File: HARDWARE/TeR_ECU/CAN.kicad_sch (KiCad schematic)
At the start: 7 parts, among them U1 SN65HVD230

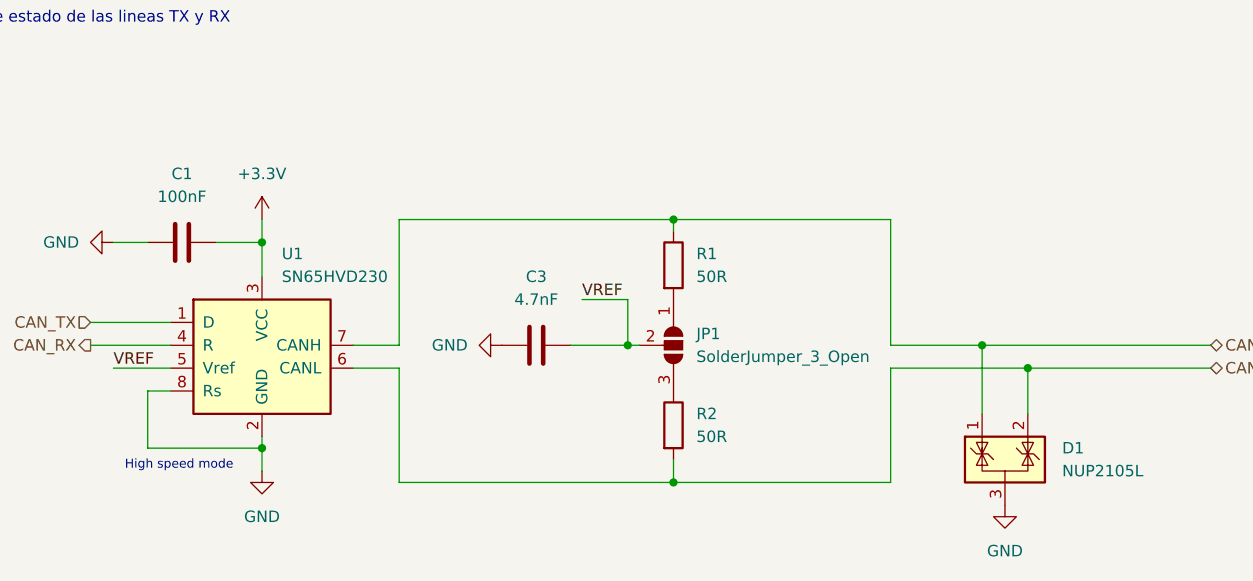
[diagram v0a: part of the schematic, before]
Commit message: Rethought layout and footprints and fixed fuse normative problem
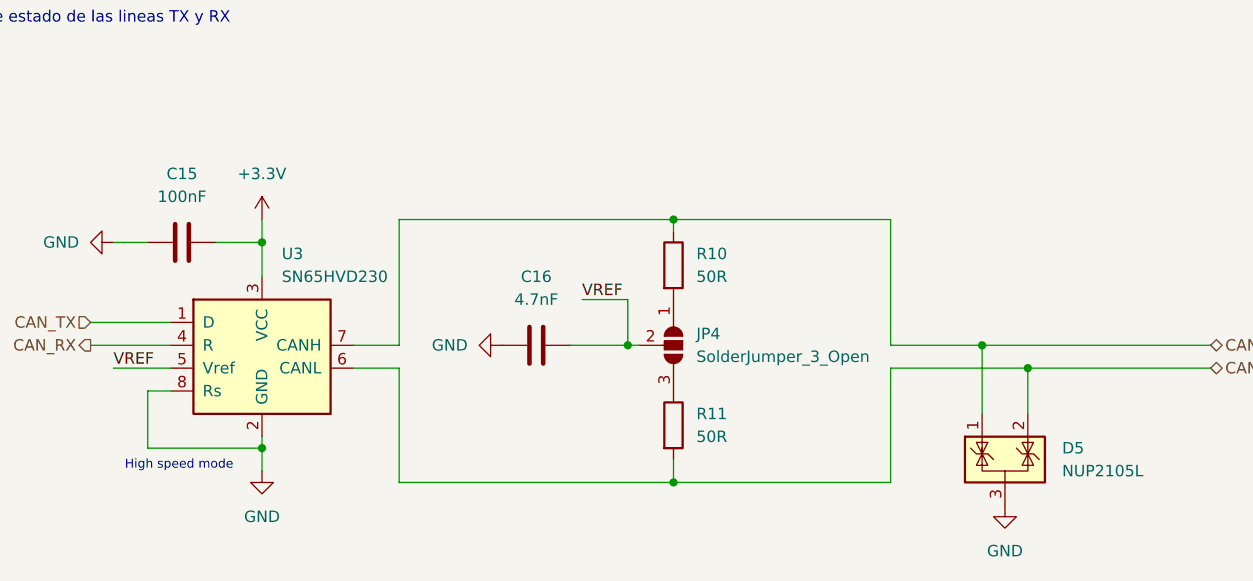
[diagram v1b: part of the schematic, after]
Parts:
- renumbered C1 to C15, C3 to C16, D1 to D5, JP1 to JP4, R1 to R10, R2 to R11, U1 to U3
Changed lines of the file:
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@@
   (symbol (lib_id "power:GND") (at 77.47 73.66 270) (unit 1)
     (in_bom yes) (on_board yes) (dnp no) (fields_autoplaced)
-    (property "Reference" "#PWR03" (at 71.12 73.66 0)
+    (property "Reference" "#PWR031" (at 71.12 73.66 0)
       (effects (font (size 1.27 1.27)) hide)
     )
@@
       (project "TeR_ECU"
         (path "/84413845-c4f3-4743-bcd2-a67649c90902/277954e6-e504-4754-bfff-78bccbfcfb29"
-          (reference "#PWR03") (unit 1)
-        )
-        (path "/84413845-c4f3-4743-bcd2-a67649c90902/5e77d980-0e17-4264-b0d2-78c6bd2786ec"
-          (reference "#PWR05") (unit 1)
+          (reference "#PWR031") (unit 1)
+        )
+        (path "/84413845-c4f3-4743-bcd2-a67649c90902/5e77d980-0e17-4264-b0d2-78c6bd2786ec"
+          (reference "#PWR024") (unit 1)
         )
       )
@@
   (symbol (lib_id "Device:R") (at 139.7 76.2 0) (unit 1)
     (in_bom yes) (on_board yes) (dnp no) (fields_autoplaced)
-    (property "Reference" "R1" (at 142.24 74.93 0)
+    (property "Reference" "R10" (at 142.24 74.93 0)
       (effects (font (size 1.27 1.27)) (justify left))
     )
@@
       (project "TeR_ECU"
         (path "/84413845-c4f3-4743-bcd2-a67649c90902/277954e6-e504-4754-bfff-78bccbfcfb29"
-          (reference "R1") (unit 1)
-        )
-        (path "/84413845-c4f3-4743-bcd2-a67649c90902/5e77d980-0e17-4264-b0d2-78c6bd2786ec"
-          (reference "R3") (unit 1)
+          (reference "R10") (unit 1)
+        )
+        (path "/84413845-c4f3-4743-bcd2-a67649c90902/5e77d980-0e17-4264-b0d2-78c6bd2786ec"
+          (reference "R8") (unit 1)
         )
       )
@@
   (symbol (lib_id "power:GND") (at 120.65 85.09 270) (unit 1)
     (in_bom yes) (on_board yes) (dnp no) (fields_autoplaced)
-    (property "Reference" "#PWR09" (at 114.3 85.09 0)
+    (property "Reference" "#PWR032" (at 114.3 85.09 0)
       (effects (font (size 1.27 1.27)) hide)
     )
@@
       (project "TeR_ECU"
         (path "/84413845-c4f3-4743-bcd2-a67649c90902/277954e6-e504-4754-bfff-78bccbfcfb29"
-          (reference "#PWR09") (unit 1)
-        )
-        (path "/84413845-c4f3-4743-bcd2-a67649c90902/5e77d980-0e17-4264-b0d2-78c6bd2786ec"
-          (reference "#PWR08") (unit 1)
+          (reference "#PWR032") (unit 1)
+        )
+        (path "/84413845-c4f3-4743-bcd2-a67649c90902/5e77d980-0e17-4264-b0d2-78c6bd2786ec"
+          (reference "#PWR025") (unit 1)
         )
       )
@@
   (symbol (lib_id "Device:R") (at 139.7 93.98 0) (unit 1)
     (in_bom yes) (on_board yes) (dnp no) (fields_autoplaced)
-    (property "Reference" "R2" (at 142.24 92.71 0)
+    (property "Reference" "R11" (at 142.24 92.71 0)
       (effects (font (size 1.27 1.27)) (justify left))
     )
@@
       (project "TeR_ECU"
         (path "/84413845-c4f3-4743-bcd2-a67649c90902/277954e6-e504-4754-bfff-78bccbfcfb29"
-          (reference "R2") (unit 1)
-        )
-        (path "/84413845-c4f3-4743-bcd2-a67649c90902/5e77d980-0e17-4264-b0d2-78c6bd2786ec"
-          (reference "R4") (unit 1)
+          (reference "R11") (unit 1)
+        )
+        (path "/84413845-c4f3-4743-bcd2-a67649c90902/5e77d980-0e17-4264-b0d2-78c6bd2786ec"
+          (reference "R9") (unit 1)
         )
       )
@@
   (symbol (lib_id "power:+3.3V") (at 93.98 71.12 0) (unit 1)
     (in_bom yes) (on_board yes) (dnp no) (fields_autoplaced)
-    (property "Reference" "#PWR02" (at 93.98 74.93 0)
+    (property "Reference" "#PWR030" (at 93.98 74.93 0)
       (effects (font (size 1.27 1.27)) hide)
     )
@@
       (project "TeR_ECU"
         (path "/84413845-c4f3-4743-bcd2-a67649c90902/277954e6-e504-4754-bfff-78bccbfcfb29"
-          (reference "#PWR02") (unit 1)
-        )
-        (path "/84413845-c4f3-4743-bcd2-a67649c90902/5e77d980-0e17-4264-b0d2-78c6bd2786ec"
-          (reference "#PWR06") (unit 1)
+          (reference "#PWR030") (unit 1)
+        )
+        (path "/84413845-c4f3-4743-bcd2-a67649c90902/5e77d980-0e17-4264-b0d2-78c6bd2786ec"
+          (reference "#PWR023") (unit 1)
         )
       )
@@
   (symbol (lib_id "Device:C") (at 124.46 85.09 270) (unit 1)
     (in_bom yes) (on_board yes) (dnp no) (fields_autoplaced)
-    (property "Reference" "C3" (at 124.46 77.47 90)
+    (property "Reference" "C16" (at 124.46 77.47 90)
       (effects (font (size 1.27 1.27)))
     )
@@
       (project "TeR_ECU"
         (path "/84413845-c4f3-4743-bcd2-a67649c90902/277954e6-e504-4754-bfff-78bccbfcfb29"
-          (reference "C3") (unit 1)
-        )
-        (path "/84413845-c4f3-4743-bcd2-a67649c90902/5e77d980-0e17-4264-b0d2-78c6bd2786ec"
-          (reference "C4") (unit 1)
+          (reference "C16") (unit 1)
+        )
+        (path "/84413845-c4f3-4743-bcd2-a67649c90902/5e77d980-0e17-4264-b0d2-78c6bd2786ec"
+          (reference "C14") (unit 1)
         )
       )
@@
   (symbol (lib_id "power:GND") (at 176.53 102.87 0) (unit 1)
     (in_bom yes) (on_board yes) (dnp no) (fields_autoplaced)
-    (property "Reference" "#PWR04" (at 176.53 109.22 0)
+    (property "Reference" "#PWR034" (at 176.53 109.22 0)
       (effects (font (size 1.27 1.27)) hide)
     )
@@
       (project "TeR_ECU"
         (path "/84413845-c4f3-4743-bcd2-a67649c90902/277954e6-e504-4754-bfff-78bccbfcfb29"
-          (reference "#PWR04") (unit 1)
-        )
-        (path "/84413845-c4f3-4743-bcd2-a67649c90902/5e77d980-0e17-4264-b0d2-78c6bd2786ec"
-          (reference "#PWR010") (unit 1)
+          (reference "#PWR034") (unit 1)
+        )
+        (path "/84413845-c4f3-4743-bcd2-a67649c90902/5e77d980-0e17-4264-b0d2-78c6bd2786ec"
+          (reference "#PWR027") (unit 1)
         )
       )
@@
   (symbol (lib_id "Device:C") (at 85.09 73.66 90) (unit 1)
     (in_bom yes) (on_board yes) (dnp no) (fields_autoplaced)
-    (property "Reference" "C1" (at 85.09 66.04 90)
+    (property "Reference" "C15" (at 85.09 66.04 90)
       (effects (font (size 1.27 1.27)))
     )
@@
       (project "TeR_ECU"
         (path "/84413845-c4f3-4743-bcd2-a67649c90902/277954e6-e504-4754-bfff-78bccbfcfb29"
-          (reference "C1") (unit 1)
-        )
-        (path "/84413845-c4f3-4743-bcd2-a67649c90902/5e77d980-0e17-4264-b0d2-78c6bd2786ec"
-          (reference "C2") (unit 1)
+          (reference "C15") (unit 1)
+        )
+        (path "/84413845-c4f3-4743-bcd2-a67649c90902/5e77d980-0e17-4264-b0d2-78c6bd2786ec"
+          (reference "C13") (unit 1)
         )
       )
@@
   (symbol (lib_id "power:GND") (at 93.98 99.06 0) (unit 1)
     (in_bom yes) (on_board yes) (dnp no) (fields_autoplaced)
-    (property "Reference" "#PWR01" (at 93.98 105.41 0)
+    (property "Reference" "#PWR033" (at 93.98 105.41 0)
       (effects (font (size 1.27 1.27)) hide)
     )
@@
       (project "TeR_ECU"
         (path "/84413845-c4f3-4743-bcd2-a67649c90902/277954e6-e504-4754-bfff-78bccbfcfb29"
-          (reference "#PWR01") (unit 1)
-        )
-        (path "/84413845-c4f3-4743-bcd2-a67649c90902/5e77d980-0e17-4264-b0d2-78c6bd2786ec"
-          (reference "#PWR07") (unit 1)
+          (reference "#PWR033") (unit 1)
+        )
+        (path "/84413845-c4f3-4743-bcd2-a67649c90902/5e77d980-0e17-4264-b0d2-78c6bd2786ec"
+          (reference "#PWR026") (unit 1)
         )
       )
@@
   (symbol (lib_id "Interface_CAN_LIN:SN65HVD230") (at 93.98 85.09 0) (unit 1)
     (in_bom yes) (on_board yes) (dnp no) (fields_autoplaced)
-    (property "Reference" "U1" (at 96.1741 74.93 0)
+    (property "Reference" "U3" (at 96.1741 74.93 0)
       (effects (font (size 1.27 1.27)) (justify left))
     )
@@
       (project "TeR_ECU"
         (path "/84413845-c4f3-4743-bcd2-a67649c90902/277954e6-e504-4754-bfff-78bccbfcfb29"
-          (reference "U1") (unit 1)
+          (reference "U3") (unit 1)
         )
         (path "/84413845-c4f3-4743-bcd2-a67649c90902/5e77d980-0e17-4264-b0d2-78c6bd2786ec"
@@
   (symbol (lib_id "Power_Protection:NUP2105L") (at 176.53 97.79 0) (unit 1)
     (in_bom yes) (on_board yes) (dnp no) (fields_autoplaced)
-    (property "Reference" "D1" (at 182.88 96.52 0)
+    (property "Reference" "D5" (at 182.88 96.52 0)
       (effects (font (size 1.27 1.27)) (justify left))
     )
@@
       (project "TeR_ECU"
         (path "/84413845-c4f3-4743-bcd2-a67649c90902/277954e6-e504-4754-bfff-78bccbfcfb29"
-          (reference "D1") (unit 1)
-        )
-        (path "/84413845-c4f3-4743-bcd2-a67649c90902/5e77d980-0e17-4264-b0d2-78c6bd2786ec"
-          (reference "D2") (unit 1)
+          (reference "D5") (unit 1)
+        )
+        (path "/84413845-c4f3-4743-bcd2-a67649c90902/5e77d980-0e17-4264-b0d2-78c6bd2786ec"
+          (reference "D4") (unit 1)
         )
       )
@@
   (symbol (lib_id "Jumper:SolderJumper_3_Open") (at 139.7 85.09 270) (unit 1)
     (in_bom yes) (on_board yes) (dnp no) (fields_autoplaced)
-    (property "Reference" "JP1" (at 142.24 83.82 90)
+    (property "Reference" "JP4" (at 142.24 83.82 90)
       (effects (font (size 1.27 1.27)) (justify left))
     )
@@
       (project "TeR_ECU"
         (path "/84413845-c4f3-4743-bcd2-a67649c90902/277954e6-e504-4754-bfff-78bccbfcfb29"
-          (reference "JP1") (unit 1)
-        )
-        (path "/84413845-c4f3-4743-bcd2-a67649c90902/5e77d980-0e17-4264-b0d2-78c6bd2786ec"
-          (reference "JP2") (unit 1)
-        )
-      )
+          (reference "JP4") (unit 1)
+        )
+        (path "/84413845-c4f3-4743-bcd2-a67649c90902/5e77d980-0e17-4264-b0d2-78c6bd2786ec"
+          (reference "JP3") (unit 1)
+        )
+      )

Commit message: Kept improving schmatic for V2
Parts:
- removed D5: NUP2105L, Package_TO_SOT_SMD:SOT-23, symbol Power_Protection:NUP2105L
- removed JP4: SolderJumper_3_Open, Jumper:SolderJumper-3_P1.3mm_Open_Pad1.0x1.5mm, symbol Jumper:SolderJumper_3_Open
- removed R11: 50R, Resistor_SMD:R_0805_2012Metric, symbol Device:R
- added D2: NUP2105L, Package_TO_SOT_SMD:SOT-23, symbol Power_Protection:NUP2105L
- added FL2: ACT45B-510-2P-TL003, ACT45B-510-2P-TL003:FIL_ACT45B-510-2P-TL003, symbol CAN_CMF:ACT45B-510-2P-TL003
- added JP2: SolderJumper_3_Open, Jumper:SolderJumper-3_P1.3mm_Open_Pad1.0x1.5mm, symbol Jumper:SolderJumper_3_Open
- added R9: 50R, Resistor_SMD:R_0805_2012Metric, symbol Device:R
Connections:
- net CAN+: now also FL2.2, R9.1; no longer R10.1, U3.7 (CANH)
- net CAN-: now also R10.2, FL2.1; no longer U3.6 (CANL)
- net GND: now also D2.3 (A)
- net VREF: now also JP2.2 (C)
- new net: JP2.1 (A), R9.2
- new net: JP2.3 (B), R10.1
- new net: D2.1 (K), FL2.4, U3.6 (CANL)
- new net: D2.2 (K), FL2.3, U3.7 (CANH)
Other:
- note added: "Isolated Can Bus transceiver"
- note removed: "Valorar leds de estado de las lineas TX y RX"

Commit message: Quick changes
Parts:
- added C24, C25: 100p, symbol Device:C
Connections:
- net CAN+: now also C25.1
- net CAN-: now also C24.1
- net GND: now also C24.2, C25.2

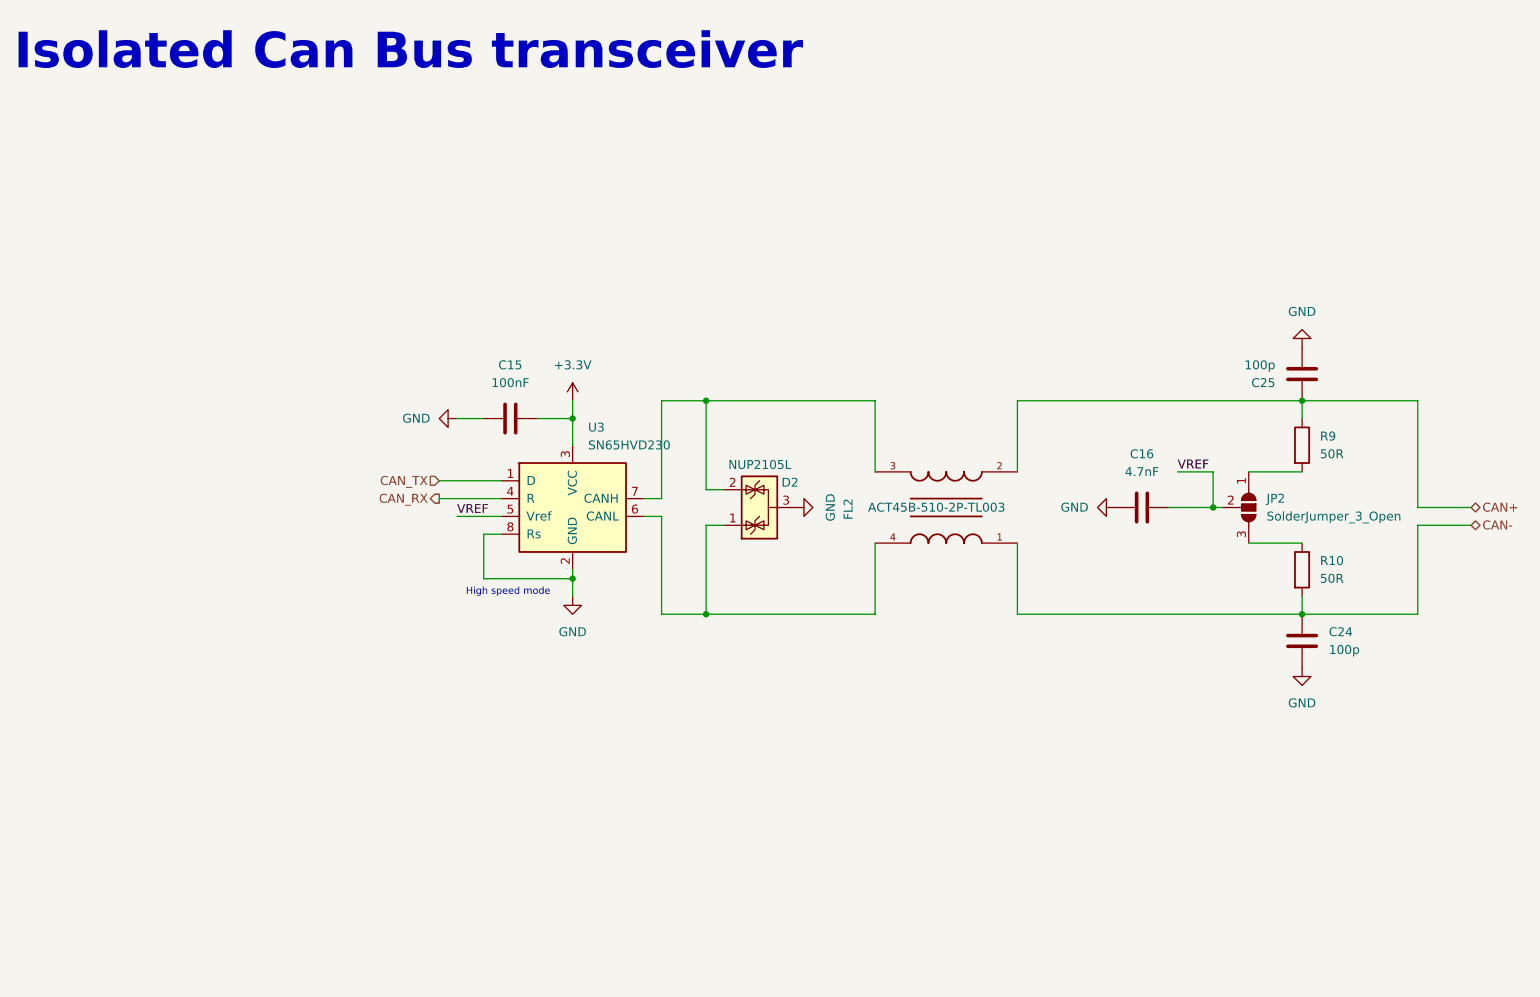
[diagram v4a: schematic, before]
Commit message: Advanced design and added IMU/GPS moduleç
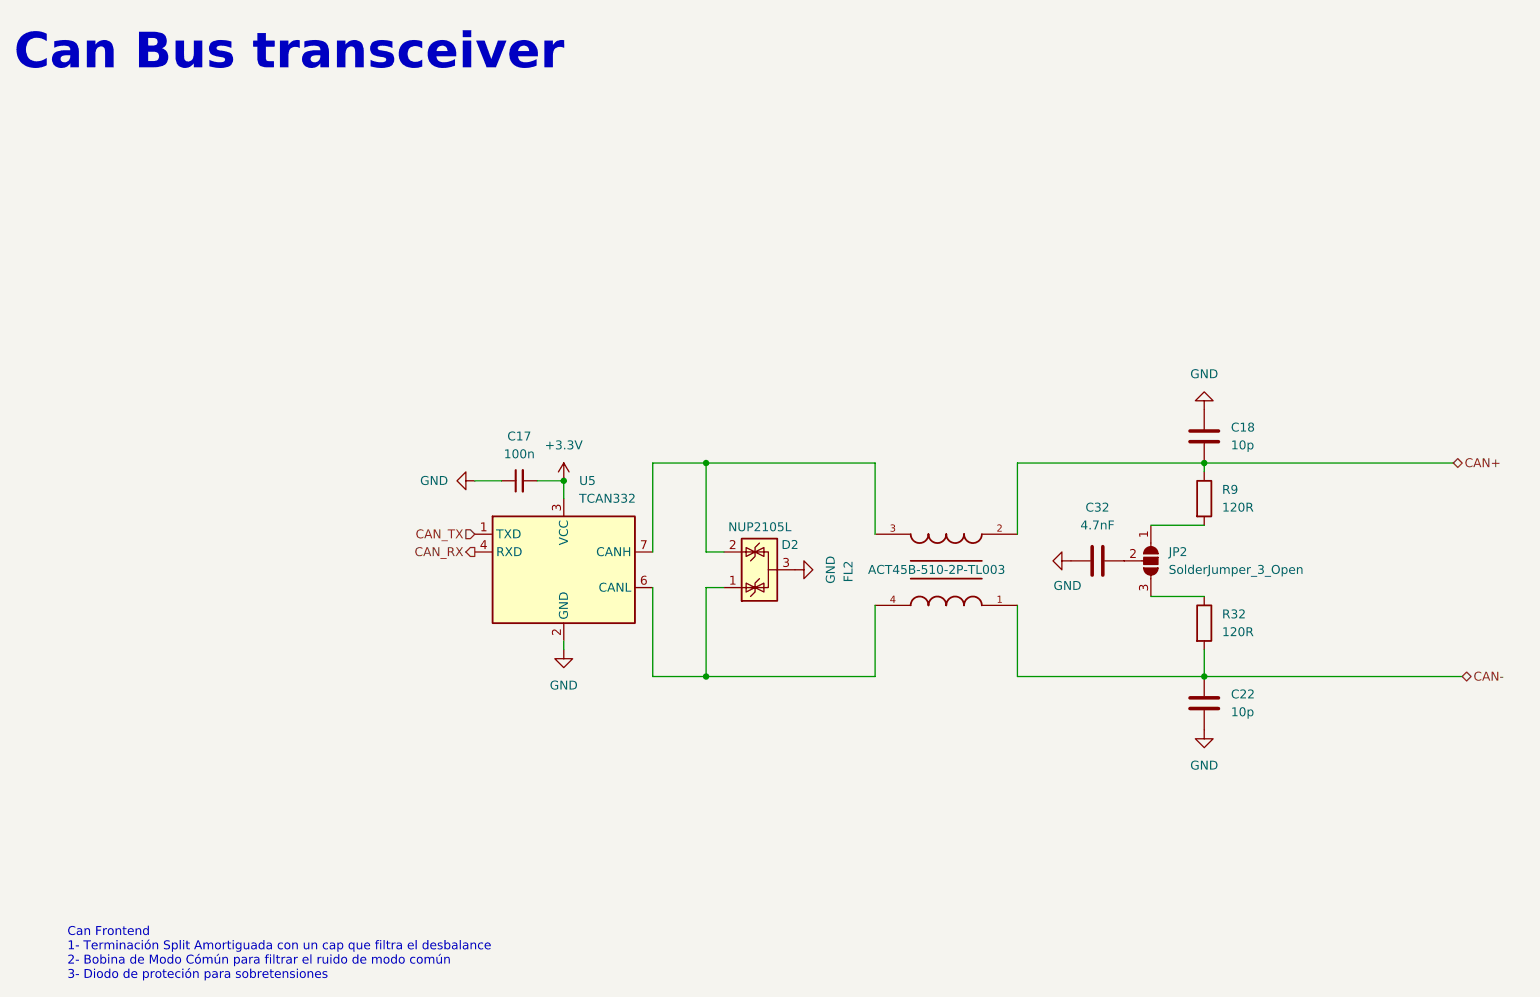
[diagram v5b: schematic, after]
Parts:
- removed C15: 100nF, Capacitor_SMD:C_0603_1608Metric, symbol Device:C
- removed C24, C25: 100p, symbol Device:C
- removed U3: SN65HVD230, Package_SO:SOIC-8_3.9x4.9mm_P1.27mm, symbol Interface_CAN_LIN:SN65HVD230
- added C17: 100n, Capacitor_SMD:C_0603_1608Metric, symbol Device:C_Small
- added C18, C22: 10p, Capacitor_SMD:C_0603_1608Metric, symbol Device:C
- added U5: TCAN332, Package_SO:SOIC-8_3.9x4.9mm_P1.27mm, symbol Interface_CAN_LIN:TCAN332
- R32: renamed from R10; value 50R -> 120R; footprint Resistor_SMD:R_0805_2012Metric -> Resistor_SMD:R_0603_1608Metric
- R9: value 50R -> 120R; footprint Resistor_SMD:R_0805_2012Metric -> Resistor_SMD:R_0603_1608Metric
- renumbered C16 to C32
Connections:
- net +3.3V: now also C17.2, U5.3 (VCC)
- net CAN+: now also C18.2
- net CAN-: now also C22.1
- net CAN_RX: now also U5.4 (RXD)
- net CAN_TX: now also U5.1 (TXD)
- net GND: now also C17.1, C18.1, C22.2, U5.2 (GND)
- net at D2.1 (K), FL2.4: now also U5.6 (CANL)
- net at D2.2 (K), FL2.3: now also U5.7 (CANH)
- net VREF: no longer names the net of C32.1, JP2.2 (C)
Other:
- note added: "Can Bus transceiver"
- note added: "Can Frontend 1- Terminación Split Amortiguada con un cap que filtra el desbalance 2- Bobina de Modo Cómún para filtrar el ruido de modo común 3- Diodo de proteción para sobretensiones"
- note removed: "High speed mode"
- note removed: "Isolated Can Bus transceiver"
- company: (none) -> Tecnun-eRacing
- title: (none) -> TeR_PEDAL
- moved on the sheet: C32, D2, FL2, JP2, R32, R9

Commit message: First layout prototype
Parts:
- FL2: footprint ACT45B-510-2P-TL003:FIL_ACT45B-510-2P-TL003 -> CAN_CMF:FIL_ACT45B-510-2P-TL003
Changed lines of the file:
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@@
 			)
 		)
-		(property "Footprint" "ACT45B-510-2P-TL003:FIL_ACT45B-510-2P-TL003"
+		(property "Footprint" "CAN_CMF:FIL_ACT45B-510-2P-TL003"
 			(at 147.32 95.25 0)
 			(effects

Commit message: Finished layout, RF design, and quick DRC check, Lookin gud
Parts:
- JP2: value SolderJumper_3_Open -> 120R Term; footprint Jumper:SolderJumper-3_P1.3mm_Open_Pad1.0x1.5mm -> Jumper:SolderJumper-3_P1.3mm_Open_RoundedPad1.0x1.5mm
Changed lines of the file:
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@@
 		(fields_autoplaced yes)
 		(property "Reference" "JP2"
-			(at 179.07 92.71 90)
+			(at 179.07 92.7099 90)
 			(effects
 				(font
@@
 			)
 		)
-		(property "Value" "SolderJumper_3_Open"
-			(at 179.07 95.25 90)
+		(property "Value" "120R Term"
+			(at 179.07 95.2499 90)
 			(effects
 				(font
@@
 			)
 		)
-		(property "Footprint" "Jumper:SolderJumper-3_P1.3mm_Open_Pad1.0x1.5mm"
+		(property "Footprint" "Jumper:SolderJumper-3_P1.3mm_Open_RoundedPad1.0x1.5mm"
 			(at 176.53 93.98 0)
 			(effects
